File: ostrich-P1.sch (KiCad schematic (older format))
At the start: 58 parts

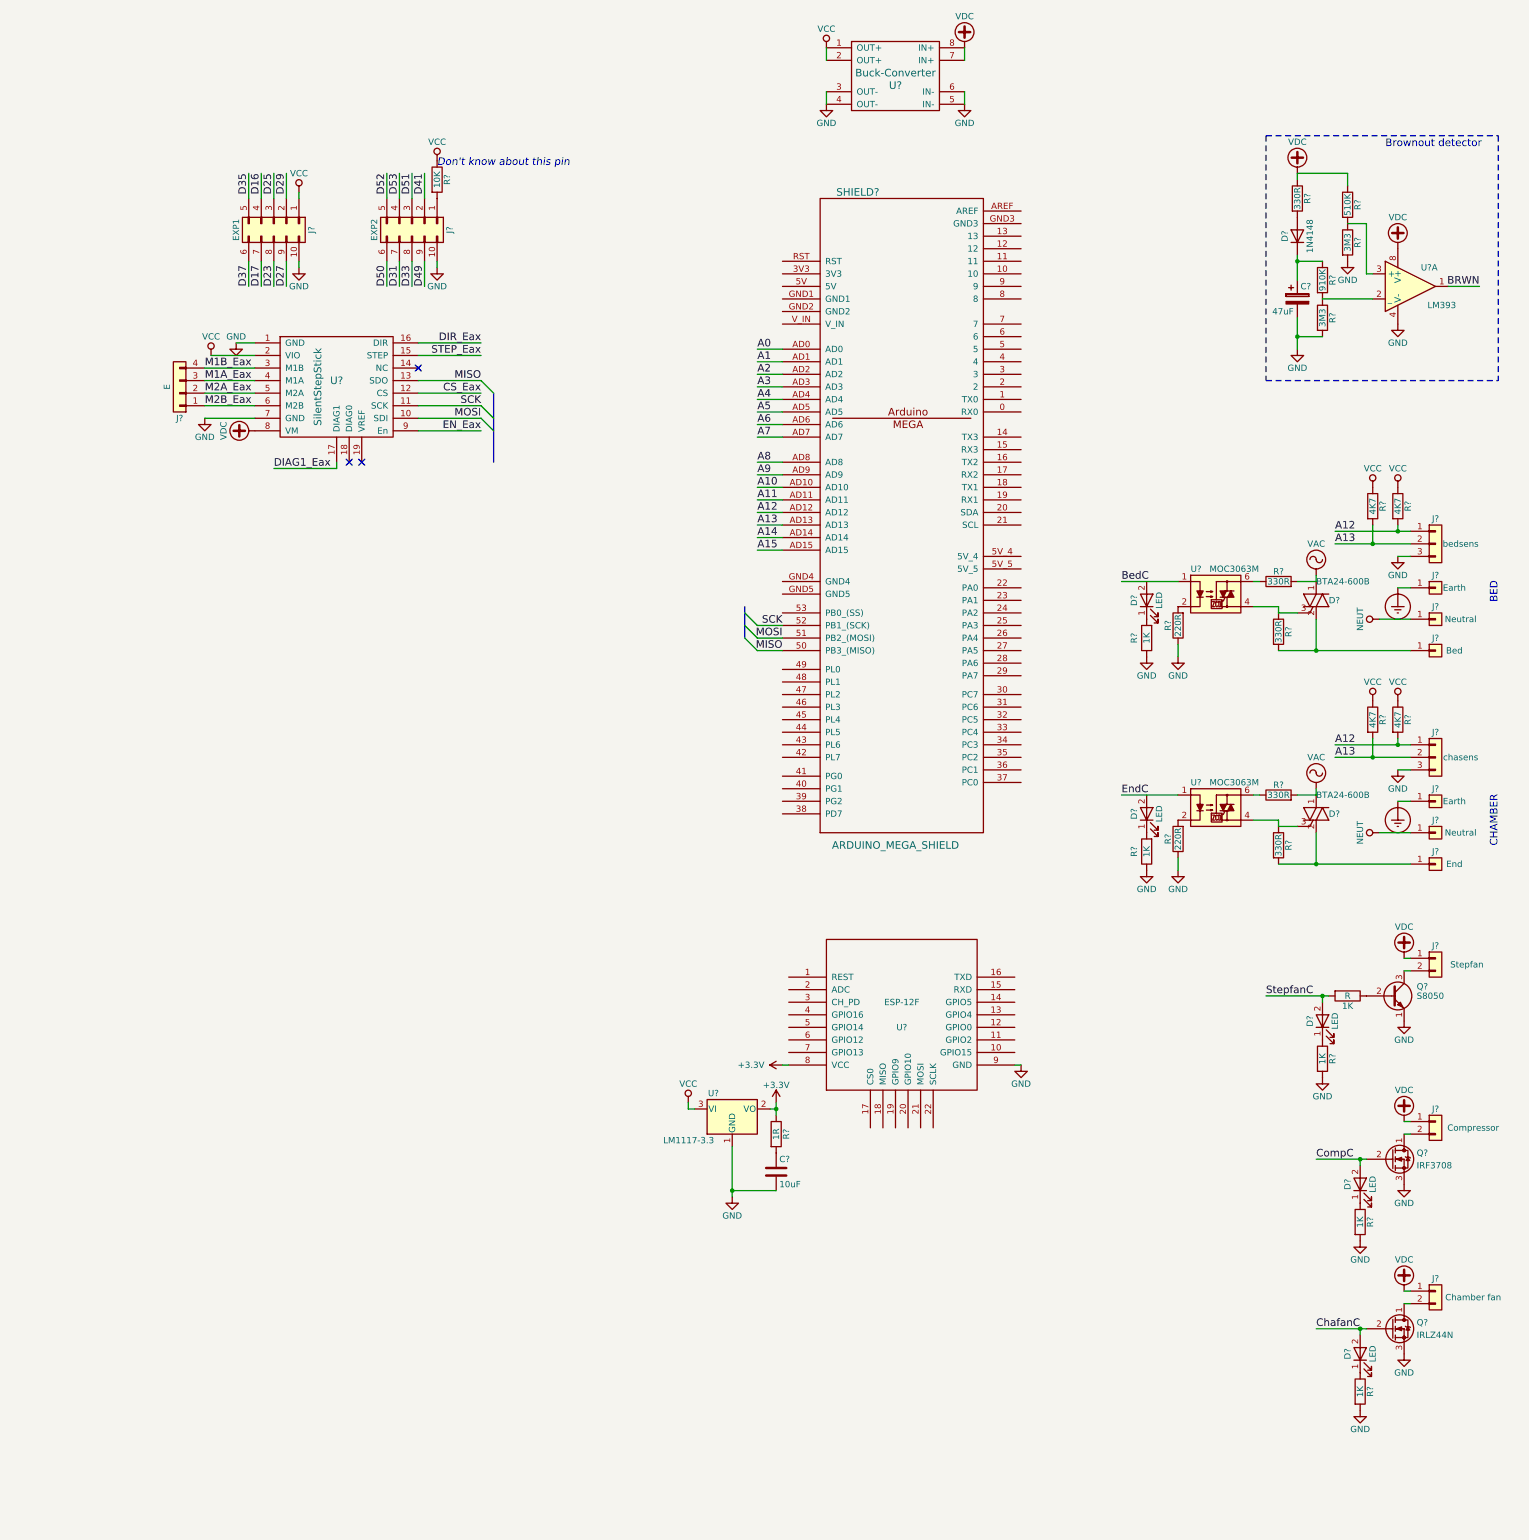
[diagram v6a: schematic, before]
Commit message: added flyback diodes and endstop OR gate.
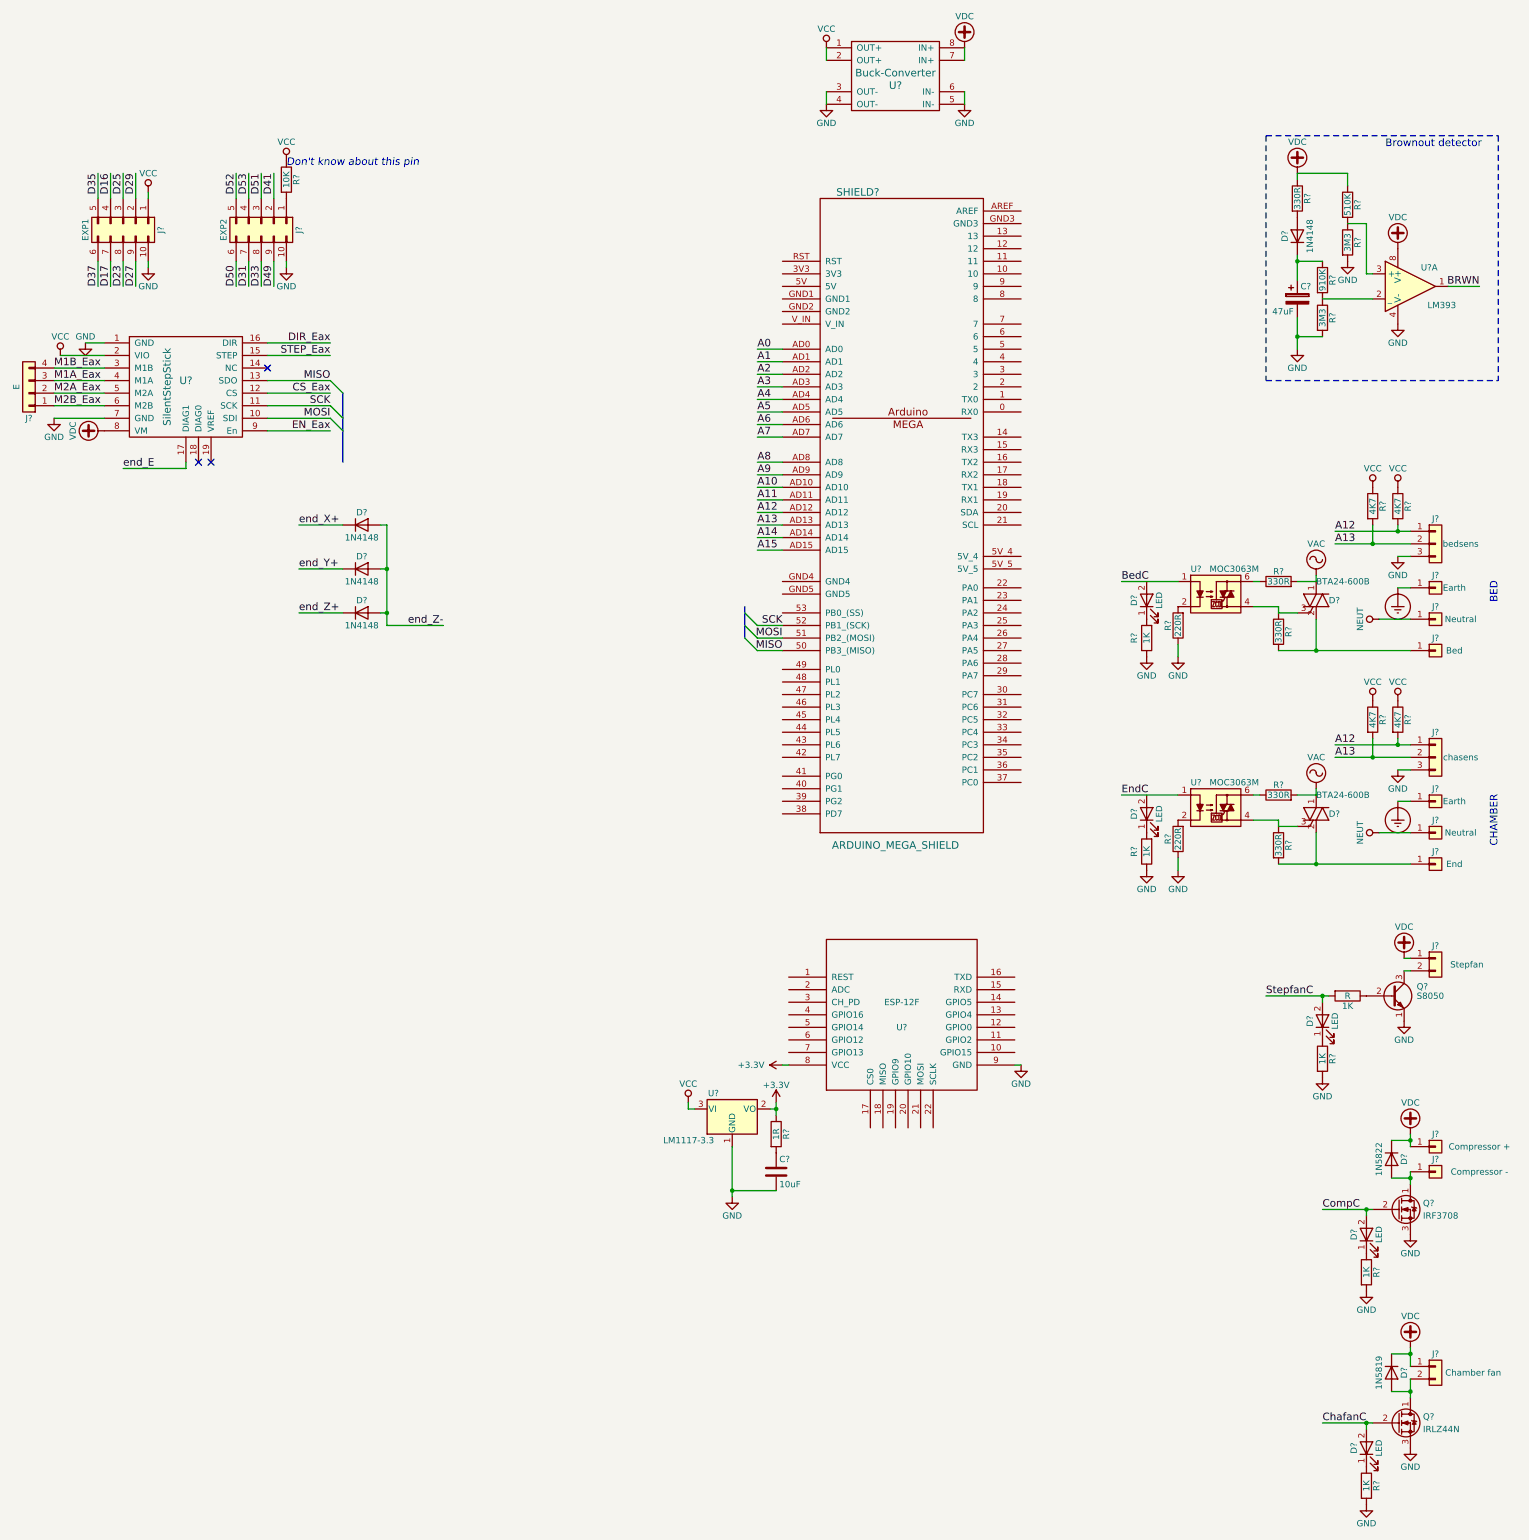
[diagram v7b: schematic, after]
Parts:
- removed J?: Compressor, symbol Conn_01x02
- added D? (x3): 1N4148, symbol D
- added D?: 1N5822, symbol D
- added D?: 1N5819, symbol D
- added J?: Compressor +, symbol Conn_01x01
- added J?: Compressor -, symbol Conn_01x01
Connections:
- net VDC: now also D?.1 (K), D?.1 (K), J?.1 (Pin_1)
- net at Q?.1 (D): now also D?.2 (A), J?.1 (Pin_1)
- net at J?.2 (Pin_2), Q?.1 (D): now also D?.2 (A)
- net DIAG1_Eax renamed end_E
- new net end_X+: D?.1 (K)
- new net end_Y+: D?.1 (K)
- new net end_Z+: D?.1 (K)
- new net end_Z-: D?.2 (A), D?.2 (A), D?.2 (A)
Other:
- moved on the sheet: D?, J?, Q?, R?, U?

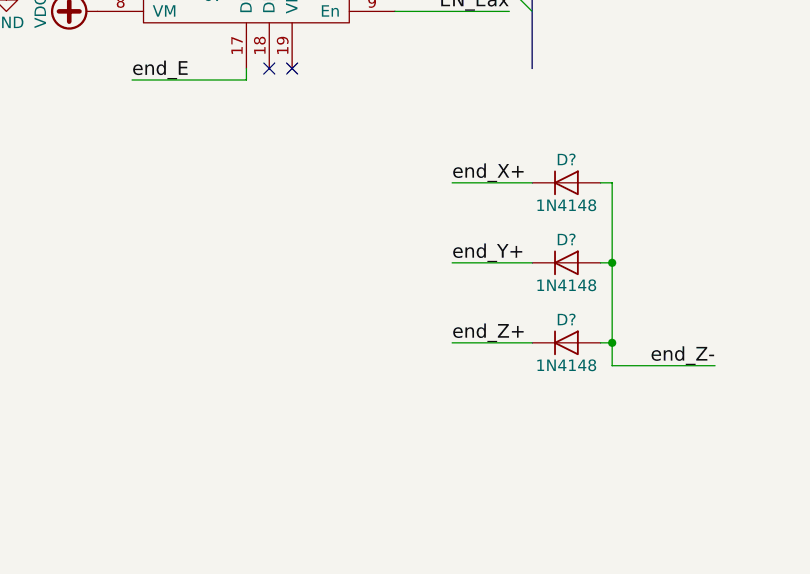
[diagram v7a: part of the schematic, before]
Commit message: added endstop headers
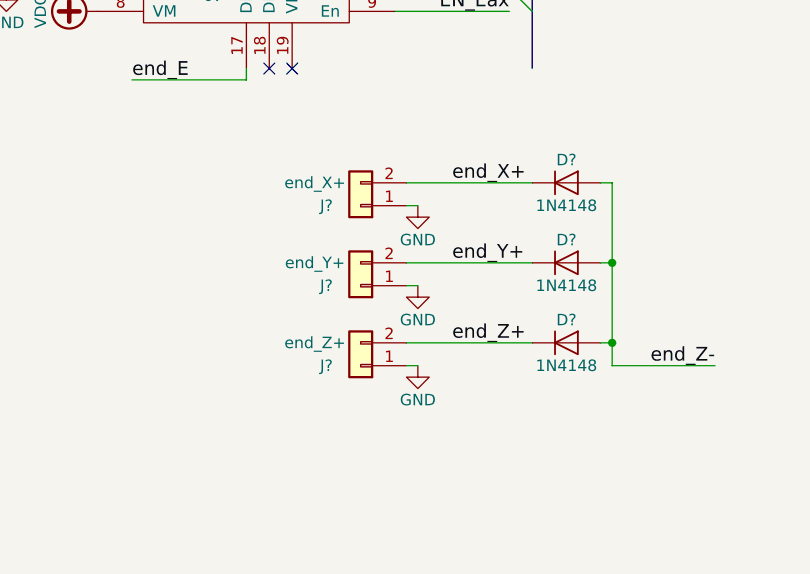
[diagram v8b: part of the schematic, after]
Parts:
- added J?: end_Y+, symbol Conn_01x02
- added J?: end_Z+, symbol Conn_01x02
- added J?: end_X+, symbol Conn_01x02
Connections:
- net GND: now also J?.1 (Pin_1), J?.1 (Pin_1), J?.1 (Pin_1)
- net end_X+: now also J?.2 (Pin_2)
- net end_Y+: now also J?.2 (Pin_2)
- net end_Z+: now also J?.2 (Pin_2)
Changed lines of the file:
@@
 end_Z-
 Wire Wire Line
-	1650 4300 2000 4300
+	1450 4300 2000 4300
 Wire Wire Line
-	1650 3950 2000 3950
+	1450 3950 2000 3950
 Wire Wire Line
-	1650 3600 2000 3600
+	1450 3600 2000 3600
 $Comp
 L D D?
@@
 	1    0    0    -1
 $EndComp
+$Comp
+L Conn_01x02 J?
+U 1 1 5AFEAB47
+P 1250 4050
+F 0 "J?" H 1400 4050 50  0000 C CNN
+F 1 "end_Y+" H 1450 3950 50  0000 C CNN
+F 2 "" H 1250 4050 50  0001 C CNN
+F 3 "" H 1250 4050 50  0001 C CNN
+	1    1250 4050
+	-1   0    0    1
+$EndComp
+$Comp
+L Conn_01x02 J?
+U 1 1 5AFEACFF
+P 1250 4400
+F 0 "J?" H 1400 4400 50  0000 C CNN
+F 1 "end_Z+" H 1450 4300 50  0000 C CNN
+F 2 "" H 1250 4400 50  0001 C CNN
+F 3 "" H 1250 4400 50  0001 C CNN
+	1    1250 4400
+	-1   0    0    1
+$EndComp
+$Comp
+L Conn_01x02 J?
+U 1 1 5AFEB203
+P 1250 3700
+F 0 "J?" H 1400 3700 50  0000 C CNN
+F 1 "end_X+" H 1450 3600 50  0000 C CNN
+F 2 "" H 1250 3700 50  0001 C CNN
+F 3 "" H 1250 3700 50  0001 C CNN
+	1    1250 3700
+	-1   0    0    1
+$EndComp
+$Comp
+L GND #PWR?
+U 1 1 5AFEB573
+P 1500 3700
+F 0 "#PWR?" H 1500 3450 50  0001 C CNN
+F 1 "GND" H 1500 3550 50  0000 C CNN
+F 2 "" H 1500 3700 50  0001 C CNN
+F 3 "" H 1500 3700 50  0001 C CNN
+	1    1500 3700
+	1    0    0    -1
+$EndComp
+Wire Wire Line
+	1450 3700 1500 3700
+Wire Wire Line
+	1450 4050 1500 4050
+Wire Wire Line
+	1450 4400 1500 4400
+$Comp
+L GND #PWR?
+U 1 1 5AFEBBC1
+P 1500 4050
+F 0 "#PWR?" H 1500 3800 50  0001 C CNN
+F 1 "GND" H 1500 3900 50  0000 C CNN
+F 2 "" H 1500 4050 50  0001 C CNN
+F 3 "" H 1500 4050 50  0001 C CNN
+	1    1500 4050
+	1    0    0    -1
+$EndComp
+$Comp
+L GND #PWR?
+U 1 1 5AFEBC95
+P 1500 4400
+F 0 "#PWR?" H 1500 4150 50  0001 C CNN
+F 1 "GND" H 1500 4250 50  0000 C CNN
+F 2 "" H 1500 4400 50  0001 C CNN
+F 3 "" H 1500 4400 50  0001 C CNN
+	1    1500 4400
+	1    0    0    -1
+$EndComp
